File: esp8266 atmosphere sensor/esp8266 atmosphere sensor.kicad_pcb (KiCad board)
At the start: 2 copper layers, 52.7 x 47.6 mm, 27 parts, among them J1 Conn_02x03_Odd_Even, J2 UJ2-MIBH-G-SMT-TR, J3 LUX sensor, J4 bme280, J5 PIR, J6 Analog in, SW1 SW_MEC_5E, U1 ESP-12F, U2 LD1117S33

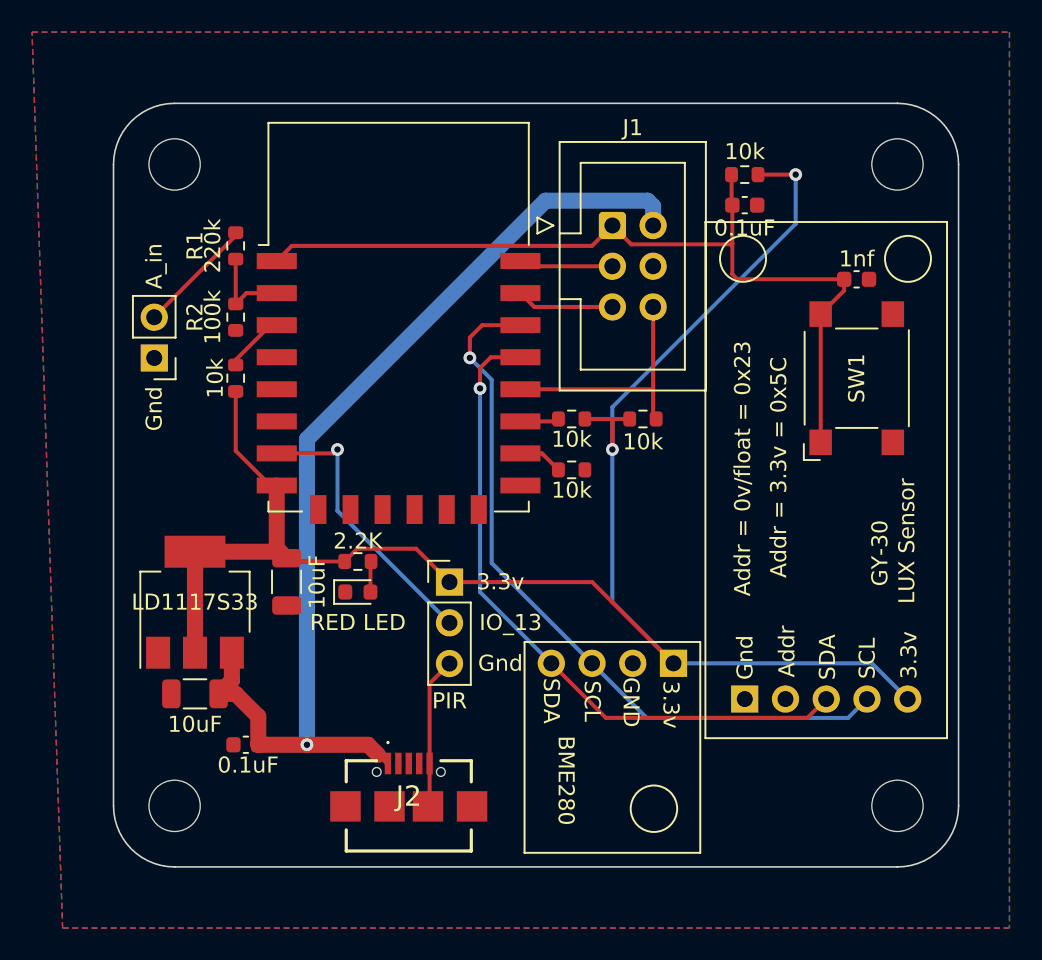
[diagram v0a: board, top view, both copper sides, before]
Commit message: added extra i2c and filtered buttons
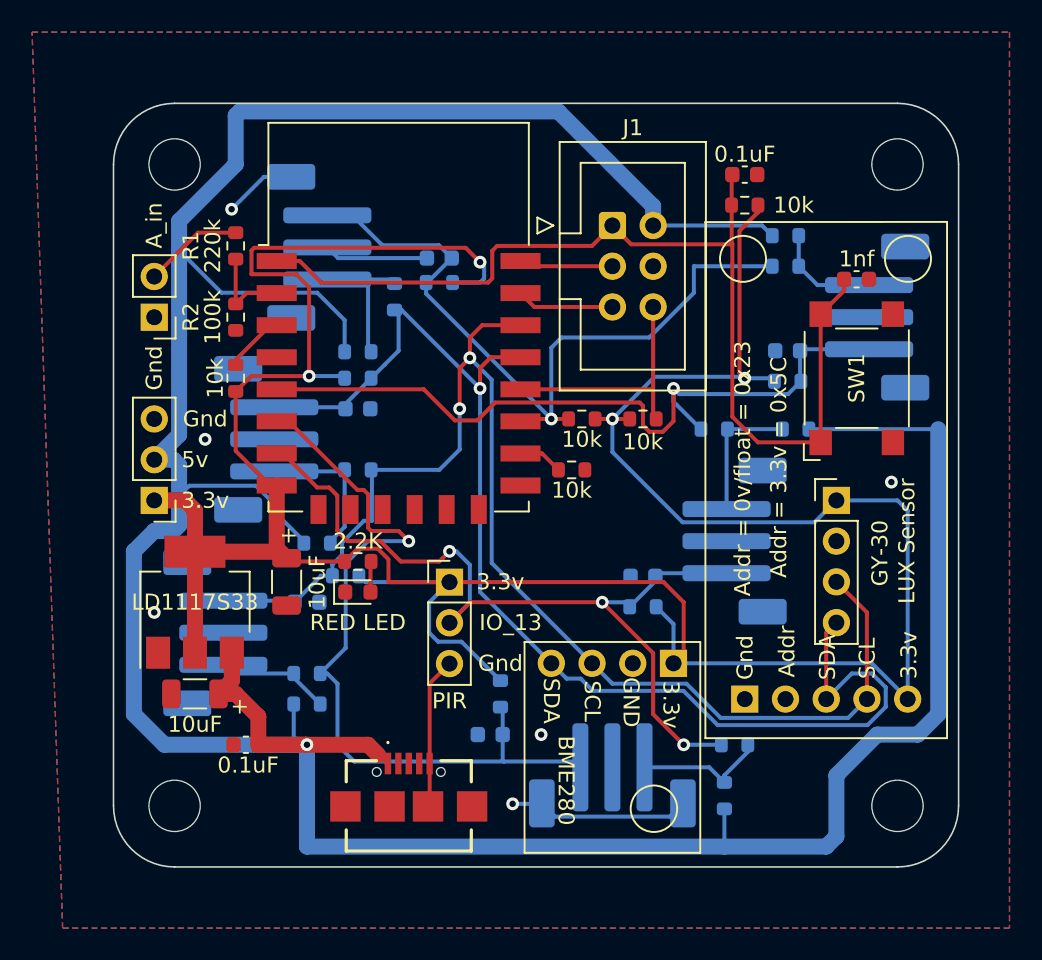
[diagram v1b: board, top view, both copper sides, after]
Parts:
- added C10: Cfilter, Capacitor_SMD:C_0603_1608Metric, B.Cu at (38.2, 11.6)
- added C11: Cfilter, Capacitor_SMD:C_0603_1608Metric, B.Cu at (11.4, 15.2)
- added C5: Cfilter, Capacitor_SMD:C_0603_1608Metric, B.Cu at (16.5, 5.84)
- added C6: Cfilter, Capacitor_SMD:C_0603_1608Metric, B.Cu at (8.26, 27.3)
- added C7: Cfilter, Capacitor_SMD:C_0603_1608Metric, B.Cu at (19.7, 35.6)
- added C8: Cfilter, Capacitor_SMD:C_0603_1608Metric, B.Cu at (29.2, 25.7)
- added G***: LOGO, Evan's misc parts:OSHW gear, B.Cu at (13.3, 31.8)
- added G***: LOGO, Evan's misc parts:Evan Logo, B.Cu at (39.4, -0.64)
- added J10: Conn_01x03, Connector_JST:JST_PH_B3B-PH-SM4-TB_1x03-1MP_P2.00mm_Vertical, B.Cu at (2.54, 29.2)
- added J11: Conn_01x03, Connector_JST:JST_PH_B3B-PH-SM4-TB_1x03-1MP_P2.00mm_Vertical, B.Cu at (27.3, 38.1)
- added J12: Conn_01x03, Connector_JST:JST_PH_B3B-PH-SM4-TB_1x03-1MP_P2.00mm_Vertical, B.Cu at (34.9, 23.5)
- added J13: Conn_01x03, Connector_JST:JST_PH_B3B-PH-SM4-TB_1x03-1MP_P2.00mm_Vertical, B.Cu at (43.8, 9.53)
- added J14: Conn_01x03, Connector_JST:JST_PH_B3B-PH-SM4-TB_1x03-1MP_P2.00mm_Vertical, B.Cu at (5.71, 17.1)
- added J7: external i2c, Connector_PinHeader_2.54mm:PinHeader_1x04_P2.54mm_Vertical, F.Cu at (41.3, 21.0)
- added J8: power, Connector_PinHeader_2.54mm:PinHeader_1x03_P2.54mm_Vertical, F.Cu at (-1.27, 21.0)
- added J9: Conn_01x03, Connector_JST:JST_PH_B3B-PH-SM4-TB_1x03-1MP_P2.00mm_Vertical, B.Cu at (9.03, 5.17)
- added R12: R5v, Resistor_SMD:R_0603_1608Metric, B.Cu at (8.26, 33.7)
- added R13: Rgpio, Resistor_SMD:R_0603_1608Metric, B.Cu at (8.26, 31.8)
- added R14: Rfilter, Resistor_SMD:R_0603_1608Metric, B.Cu at (10.7, 25.7)
- added R15: R5v, Resistor_SMD:R_0603_1608Metric, B.Cu at (34.3, 39.4)
- added R16: Rgpio, Resistor_SMD:R_0603_1608Metric, B.Cu at (34.9, 36.2)
- added R17: Rfilter, Resistor_SMD:R_0603_1608Metric, B.Cu at (20.3, 33.0)
- added R18: R5v, Resistor_SMD:R_0603_1608Metric, B.Cu at (38.7, 16.5)
- added R19: Rgpio, Resistor_SMD:R_0603_1608Metric, B.Cu at (33.7, 16.5)
- added R20: Rfilter, Resistor_SMD:R_0603_1608Metric, B.Cu at (29.2, 27.6)
- added R21: R5v, Resistor_SMD:R_0603_1608Metric, B.Cu at (38.1, 4.45)
- added R22: Rgpio, Resistor_SMD:R_0603_1608Metric, B.Cu at (38.1, 6.35)
- added R23: Rfilter, Resistor_SMD:R_0603_1608Metric, B.Cu at (38.2, 13.5)
- added R24: R5v, Resistor_SMD:R_0603_1608Metric, B.Cu at (8.89, 23.6)
- added R25: Rgpio, Resistor_SMD:R_0603_1608Metric, B.Cu at (11.4, 19.1)
- added R26: Rfilter, Resistor_SMD:R_0603_1608Metric, B.Cu at (11.4, 13.3)
- added R4: R5v, Resistor_SMD:R_0603_1608Metric, B.Cu at (11.4, 11.7)
- added R6: Rgpio, Resistor_SMD:R_0603_1608Metric, B.Cu at (13.7, 8.26)
- added R7: Rfilter, Resistor_SMD:R_0603_1608Metric, B.Cu at (16.5, 7.37)
- moved J6 2.54 mm to (-1.27, 9.53)
- moved C9 1.91 mm to (35.6, 0.64)
- moved R9 1.91 mm to (35.6, 2.54)
- moved R11 0.63 mm to (25.4, 15.9)
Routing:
- net +5V: track 64.5 -> 213.8 mm
- net +3V3: track 110.4 -> 190.8 mm, vias 2 -> 4
- net /ESP_IO12: track 0.00 -> 49.0 mm, vias 0 -> 1
- net /ESP_IO14: track 0.00 -> 47.7 mm, vias 0 -> 1
- net /ESP_IO2: track 2.43 -> 47.2 mm, vias 0 -> 1
- net /ESP_IO13: track 17.6 -> 53.2 mm, vias 1 -> 3
- net /ESP_IO5: track 46.0 -> 81.6 mm, vias 1 -> 2
- net /ESP_IO4: track 42.1 -> 76.1 mm
- net GND: track 9.47 -> 31.9 mm, vias 0 -> 6
- net /ESP_RST: track 54.0 -> 64.1 mm
- net Net-(J14-Pad3): track 0.00 -> 9.24 mm
- net Net-(J9-Pad3): track 0.00 -> 8.44 mm
- net Net-(J12-Pad3): track 0.00 -> 8.44 mm
- net Net-(J11-Pad3): track 0.00 -> 8.33 mm
- net Net-(J10-Pad3): track 0.00 -> 7.20 mm
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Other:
- board text added: "+"
- board text added: "5v"
- board text added: "Atmosphere sensor board v2"
- board text added: "IO_0"
- board text added: "IO_1"
- board text added: "IO_12"
- board text added: "IO_2"
- board text added: "IO_3"
- board text added: "IO_4"
- board text added: "IO_5"
- board text added: "Rst"
- board text added: "Rx"
- board text added: "SCL"
- board text added: "SDA"
- board text added: "Tx"
- board text added: "abzman2k.wordpress.com"
